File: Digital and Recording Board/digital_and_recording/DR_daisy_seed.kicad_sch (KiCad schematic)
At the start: 2 parts, among them U1 Daisy_Seed, U2 Daisy_Seed_Recording

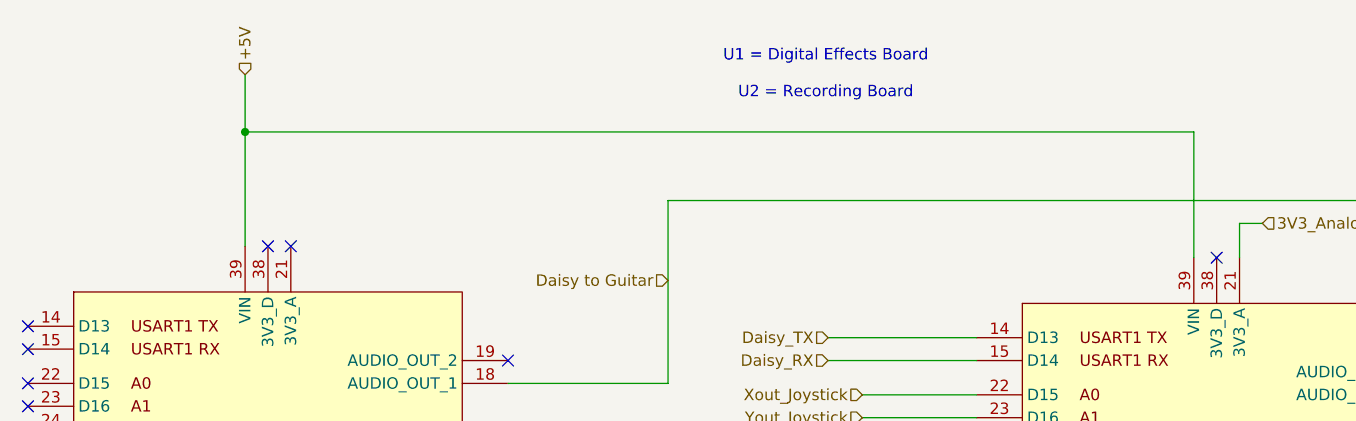
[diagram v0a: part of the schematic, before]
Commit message: modified power for proper amp rating of daisy seed
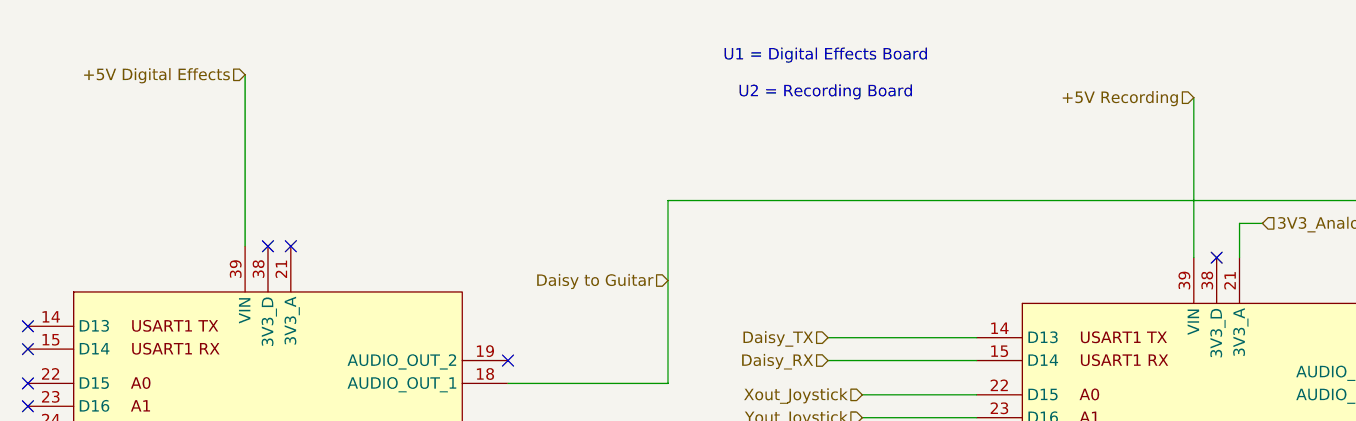
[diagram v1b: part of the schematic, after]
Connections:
- net +5V renamed +5V Digital Effects
- net +5V Digital Effects: no longer U2.39 (VIN)
- new net +5V Recording: U2.39 (VIN)
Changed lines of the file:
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@@
 		(color 0 0 0 0)
 	)
-	(junction
-		(at 80.01 25.4)
-		(diameter 0)
-		(color 0 0 0 0)
-	)
 	(no_connect
 		(at 55.88 86.36)
@@
 	(wire
 		(pts
-			(xy 80.01 25.4) (xy 80.01 38.1)
+			(xy 80.01 19.05) (xy 80.01 38.1)
 		)
 		(stroke
@@
 	(wire
 		(pts
-			(xy 80.01 19.05) (xy 80.01 25.4)
-		)
-		(stroke
-			(width 0)
-			(type default)
-		)
-	)
-	(wire
-		(pts
 			(xy 81.28 113.03) (xy 83.82 113.03)
 		)
@@
 	(wire
 		(pts
-			(xy 80.01 25.4) (xy 185.42 25.4)
-		)
-		(stroke
-			(width 0)
-			(type default)
-		)
-	)
-	(wire
-		(pts
 			(xy 146.05 93.98) (xy 161.29 93.98)
 		)
@@
 	(wire
 		(pts
-			(xy 185.42 39.37) (xy 185.42 25.4)
+			(xy 185.42 21.59) (xy 185.42 39.37)
 		)
 		(stroke
@@
 		)
 	)
-	(hierarchical_label "+5V"
-		(shape input)
-		(at 80.01 19.05 90)
+	(hierarchical_label "Daisy_RX"
+		(shape input)
+		(at 144.78 50.8 180)
+		(effects
+			(font
+				(size 1.27 1.27)
+			)
+			(justify right)
+		)
+	)
+	(hierarchical_label "Xout_Joystick"
+		(shape input)
+		(at 148.59 54.61 180)
+		(effects
+			(font
+				(size 1.27 1.27)
+			)
+			(justify right)
+		)
+	)
+	(hierarchical_label "+5V Digital Effects"
+		(shape input)
+		(at 80.01 19.05 180)
+		(effects
+			(font
+				(size 1.27 1.27)
+			)
+			(justify right)
+		)
+	)
+	(hierarchical_label "Guitar to Daisy"
+		(shape input)
+		(at 115.57 63.5 0)
 		(effects
 			(font
@@
 		)
 	)
-	(hierarchical_label "Daisy_RX"
-		(shape input)
-		(at 144.78 50.8 180)
-		(effects
-			(font
-				(size 1.27 1.27)
-			)
-			(justify right)
-		)
-	)
-	(hierarchical_label "Xout_Joystick"
-		(shape input)
-		(at 148.59 54.61 180)
-		(effects
-			(font
-				(size 1.27 1.27)
-			)
-			(justify right)
-		)
-	)
-	(hierarchical_label "Guitar to Daisy"
-		(shape input)
-		(at 115.57 63.5 0)
-		(effects
-			(font
-				(size 1.27 1.27)
-			)
-			(justify left)
-		)
-	)
+	(hierarchical_label "+5V Recording"
+		(shape input)
+		(at 185.42 21.59 180)
+		(effects
+			(font
+				(size 1.27 1.27)
+			)
+			(justify right)
+		)
+	)

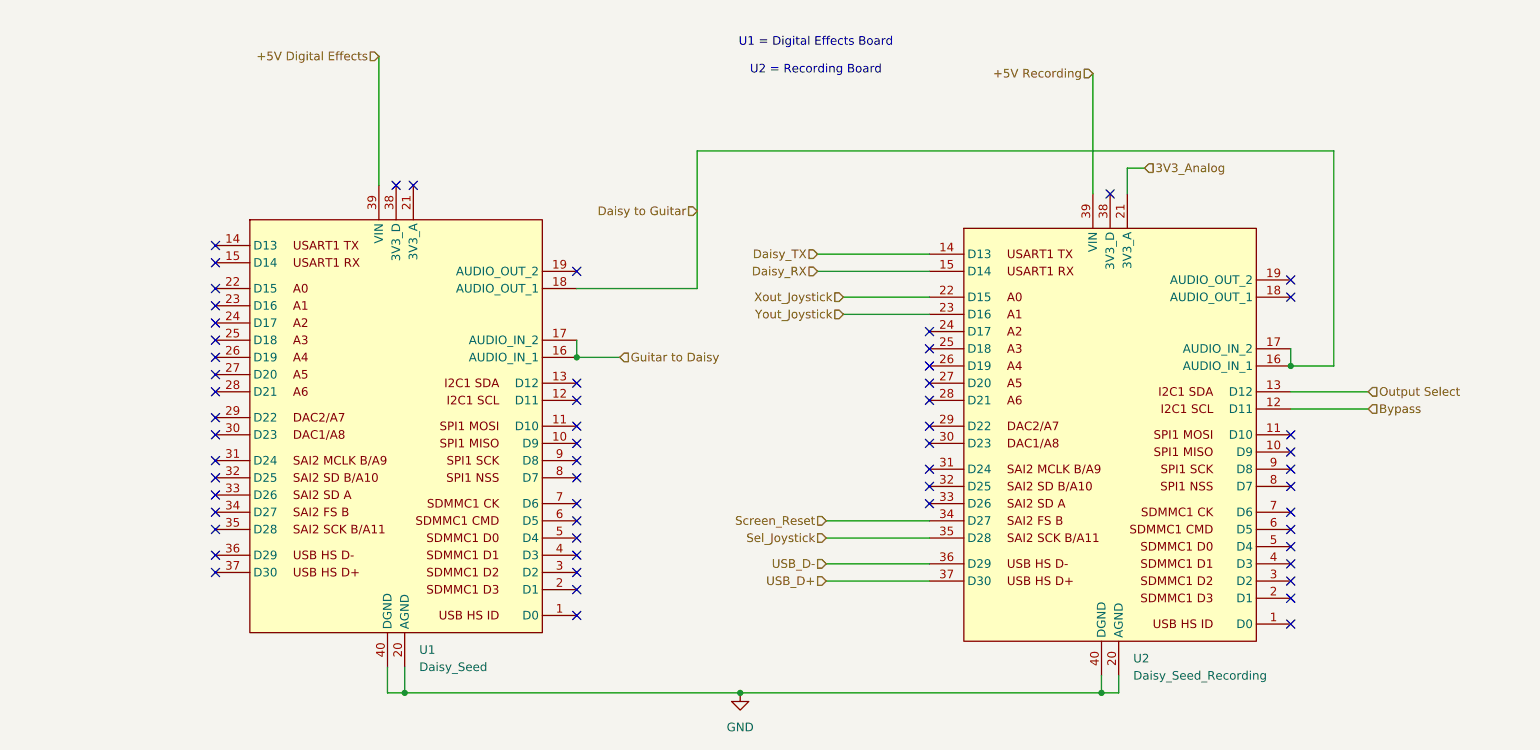
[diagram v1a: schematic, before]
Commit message: layout for digital board is essentially complete
current draw for the screen may fuck us if it is too high
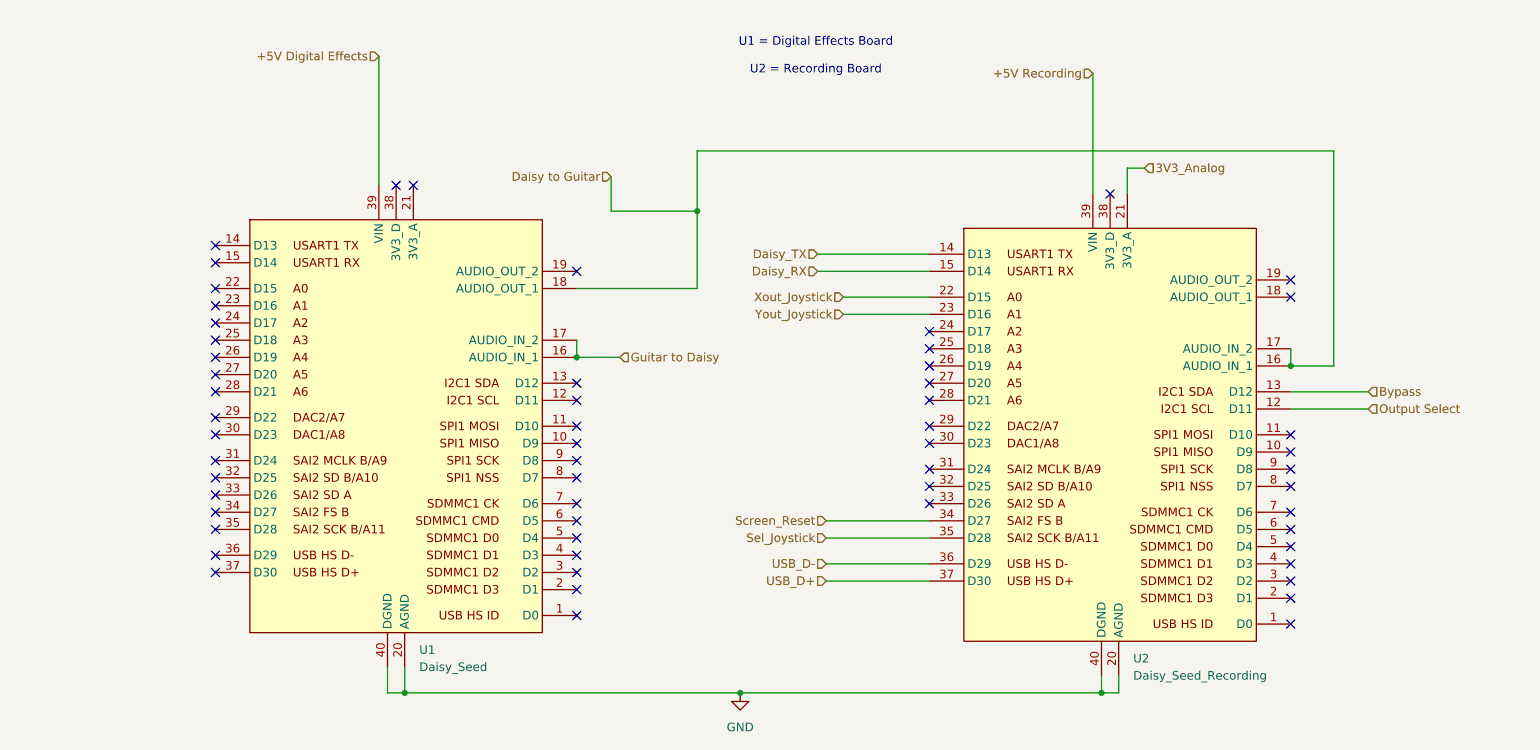
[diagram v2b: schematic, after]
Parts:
- U1, U2: footprint Daisy-Boards:DAISY_SEED -> Kyle's Footprints:DAISY_SEED
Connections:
- net Bypass: now also U2.13 (D12); no longer U2.12 (D11)
- net Output Select: now also U2.12 (D11); no longer U2.13 (D12)

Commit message: im pushing in case kicad crashes again
also the board was significantly updated
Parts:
- added R1, R2: R, Resistor_SMD:R_0603_1608Metric, symbol Device:R
- added R3, R4, R5, R6: 0, Resistor_SMD:R_0603_1608Metric, symbol Device:R
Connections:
- net Bypass: now also U2.11 (D10); no longer U2.13 (D12)
- net Daisy_RX: now also R4.1, R6.1; no longer U2.15 (D14)
- net Daisy_TX: now also R3.1, R5.1; no longer U2.14 (D13)
- net Output Select: now also U2.10 (D9); no longer U2.12 (D11)
- net Sel_Joystick: now also U1.35 (D28); no longer U2.35 (D28)
- net Xout_Joystick: now also U1.22 (D15); no longer U2.22 (D15)
- net Yout_Joystick: now also U1.23 (D16); no longer U2.23 (D16)
- net I2C_SCL: now reaches U1.12 (D11)
- net I2C_SCL: now also U2.12 (D11), R2.2
- net I2C_SDA: now reaches U1.13 (D12)
- net I2C_SDA: now also U2.13 (D12), R1.2
- net at U1.14 (D13): now also R5.2
- net at U1.15 (D14): now also R6.2
- net 3V3: now reaches U1.38 (3V3_D)
- net 3V3: now also R1.1, R2.1
- new net: R3.2, U2.14 (D13)
- new net: R4.2, U2.15 (D14)
- no-connect marks 58 -> 51
